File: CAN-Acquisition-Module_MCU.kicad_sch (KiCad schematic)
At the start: 25 parts

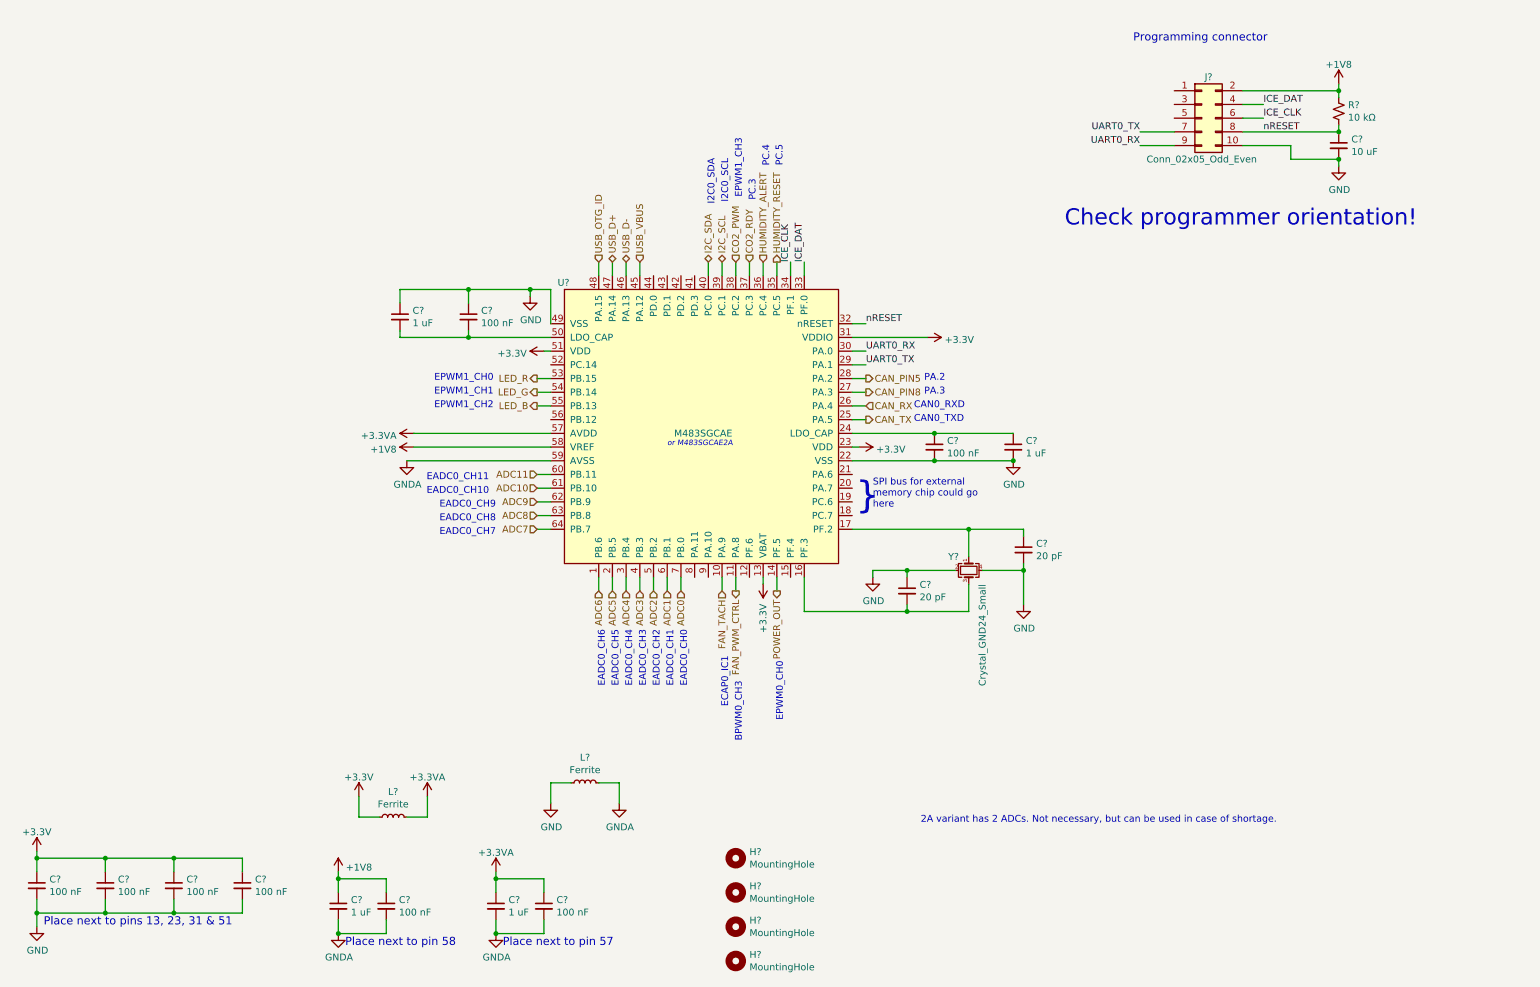
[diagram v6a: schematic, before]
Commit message: Added screen sections and annotations
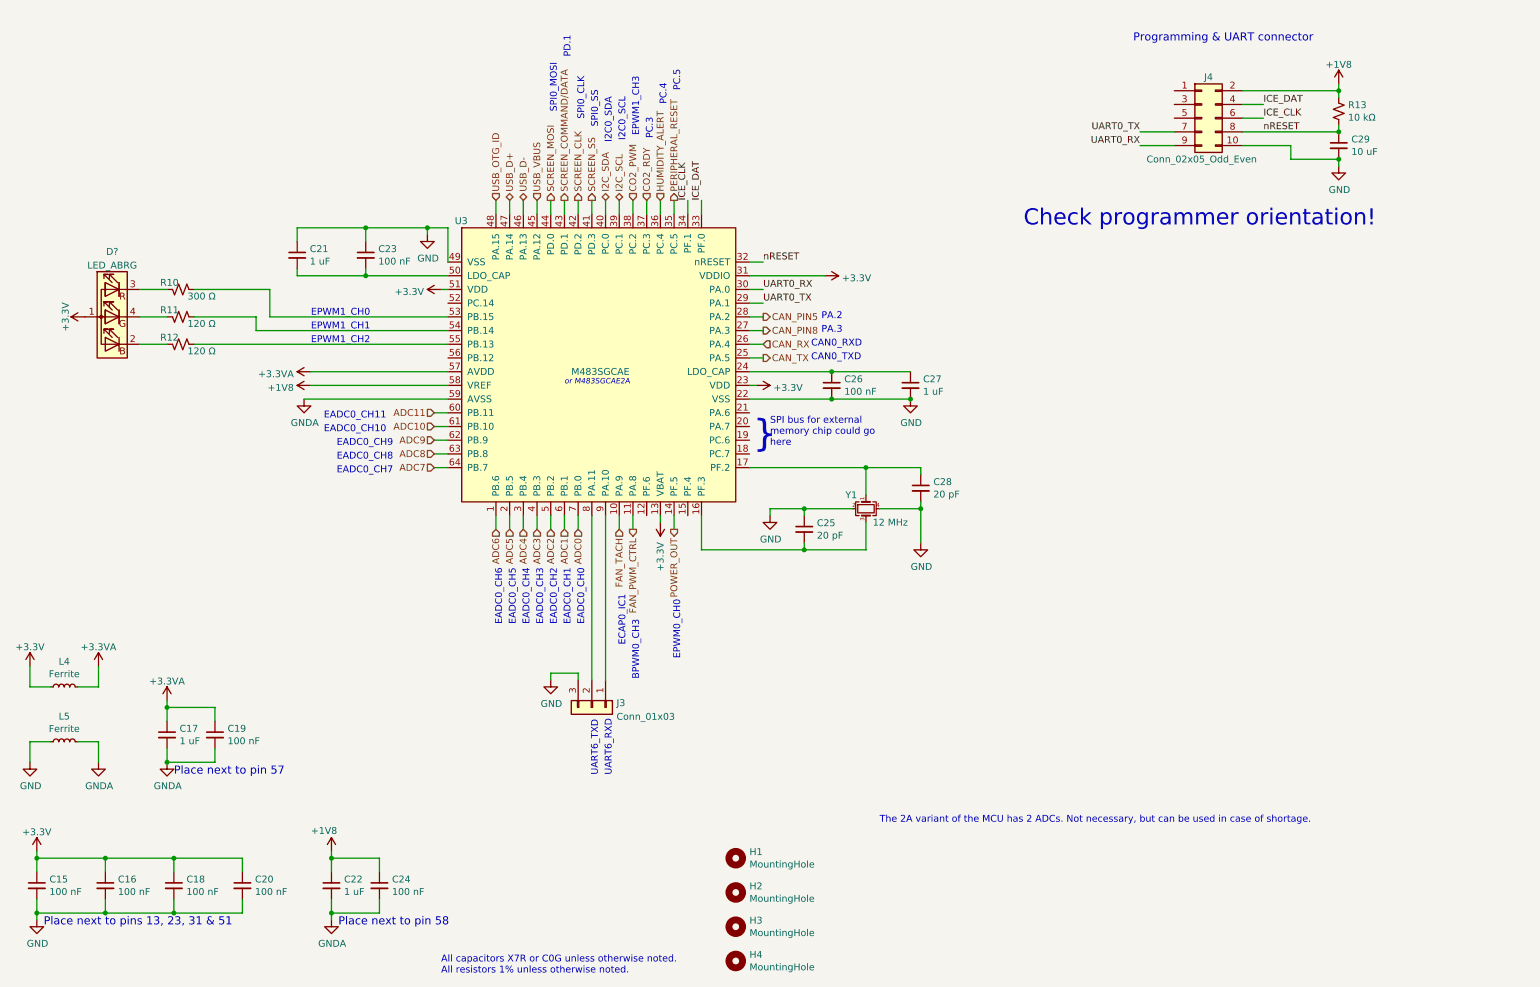
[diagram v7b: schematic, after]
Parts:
- removed H? (x3): MountingHole, symbol Mechanical:MountingHole
- added D?: LED_ABRG, CAN-Acquisition-Module:LED_RGB_Wuerth-PLCC4_3.2x2.8mm_150141M173100, symbol Device:LED_ABRG
- added H2, H3, H4: MountingHole, MountingHole:MountingHole_3.2mm_M3, symbol Mechanical:MountingHole
- added J3: Conn_01x03, Connector_PinHeader_1.27mm:PinHeader_1x03_P1.27mm_Vertical, symbol Connector_Generic:Conn_01x03
- added R10: 300 Ω, Resistor_SMD:R_0603_1608Metric, symbol Device:R_Small_US
- added R11, R12: 120 Ω, Resistor_SMD:R_0603_1608Metric, symbol Device:R_Small_US
- C15, C16, C18, C19, C20, C23, C24, C26: renamed from C?; Mfr. (none) -> KYOCERA AVX; P/N (none) -> 0402YC104KAT2A; Rated Voltage (none) -> 16V
- C17, C21, C22, C27: renamed from C?; Mfr. (none) -> Samsung Electro-Mechanics; P/N (none) -> CL10B105KA8NNNC; Rated Voltage (none) -> 25V
- C29: renamed from C?; footprint Capacitor_SMD:C_1206_3216Metric -> Capacitor_SMD:C_0805_2012Metric; Mfr. (none) -> TDK Corporation; P/N (none) -> C2012X7R0J106K125AB; Rated Voltage (none) -> 6.3V
- H1: renamed from H?; footprint (none) -> MountingHole:MountingHole_3.2mm_M3
- J4: renamed from J?; footprint (none) -> Connector_PinSocket_2.54mm:PinSocket_2x05_P2.54mm_Vertical
- Y1: renamed from Y?; value Crystal_GND24_Small -> 12 MHz
- gave numbers to parts that had none: 6
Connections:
- net +3V3: now also D?.1 (A)
- net GND: now also J3.3 (Pin_3)
- net SCREEN_SS: now reaches U3.41 (PD.3)
- net SCREEN_CLK: now reaches U3.42 (PD.2)
- net SCREEN_COMMAND/DATA: now reaches U3.43 (PD.1)
- net SCREEN_MOSI: now reaches U3.44 (PD.0)
- net at U3.8 (PA.11): now also J3.2 (Pin_2)
- net at U3.9 (PA.10): now also J3.1 (Pin_1)
- net HUMIDITY_RESET renamed PERIPHERAL_RESET
- net LED_B: no longer names the net of U3.55 (PB.13)
- net LED_B: now also R12.1
- net LED_G: no longer names the net of U3.54 (PB.14)
- net LED_G: now also R11.1
- net LED_R: no longer names the net of U3.53 (PB.15)
- net LED_R: now also R10.1
- new net: D?.4 (GK), R11.2
- new net: D?.2 (BK), R12.2
- new net: D?.3 (RK), R10.2
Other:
- note added: "All capacitors X7R or C0G unless otherwise noted. All resistors 1% unless otherwise noted."
- note added: "PD.1"
- note added: "Programming & UART connector"
- note added: "SPI0_CLK"
- note added: "SPI0_MOSI"
- note added: "SPI0_SS"
- note added: "The 2A variant of the MCU has 2 ADCs. Not necessary, but can be used in case of shortage."
- note added: "UART6_RXD"
- note added: "UART6_TXD"
- note removed: "2A variant has 2 ADCs. Not necessary, but can be used in case of shortage."
- note removed: "Programming connector"
- moved on the sheet: C17, C19, C21, C22, C23, C24, C25, C26, C27, C28, L4, L5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

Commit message: PCB started
Placement well advanced
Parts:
- added C43: 1 uF, Capacitor_SMD:C_0603_1608Metric, symbol Device:C_Small
- added C45: 100 nF, Capacitor_SMD:C_0402_1005Metric, symbol Device:C_Small
- gave numbers to parts that had none: 1
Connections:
- net +1V8: no longer J4.2 (Pin_2), R13.1
- net +3V3: now also J4.2 (Pin_2), R13.1, C43.1, C45.1
- net GND: now also C43.2, C45.2
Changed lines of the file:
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@@
   (junction (at 176.53 86.36) (diameter 0) (color 0 0 0 0)
   )
+  (junction (at 27.94 118.11) (diameter 0) (color 0 0 0 0)
+  )
   (junction (at 193.04 106.68) (diameter 0) (color 0 0 0 0)
   )
@@
   (junction (at 53.34 143.51) (diameter 0) (color 0 0 0 0)
   )
+  (junction (at 27.94 107.95) (diameter 0) (color 0 0 0 0)
+  )
   (junction (at 270.51 41.91) (diameter 0) (color 0 0 0 0)
   )
@@
     (stroke (width 0) (type default) (color 0 0 0 0))
   )
+  (wire (pts (xy 36.83 107.95) (xy 27.94 107.95))
+    (stroke (width 0) (type default) (color 0 0 0 0))
+  )
   (wire (pts (xy 161.29 76.2) (xy 163.83 76.2))
     (stroke (width 0) (type default) (color 0 0 0 0))
@@
     (stroke (width 0) (type default) (color 0 0 0 0))
   )
+  (wire (pts (xy 27.94 118.11) (xy 36.83 118.11))
+    (stroke (width 0) (type default) (color 0 0 0 0))
+  )
+  (wire (pts (xy 27.94 110.49) (xy 27.94 107.95))
+    (stroke (width 0) (type default) (color 0 0 0 0))
+  )
   (wire (pts (xy 90.17 63.5) (xy 105.41 63.5))
     (stroke (width 0) (type default) (color 0 0 0 0))
@@
     (stroke (width 0) (type default) (color 0 0 0 0))
   )
+  (wire (pts (xy 27.94 118.11) (xy 27.94 119.38))
+    (stroke (width 0) (type default) (color 0 0 0 0))
+  )
   (wire (pts (xy 121.92 107.95) (xy 121.92 110.49))
     (stroke (width 0) (type default) (color 0 0 0 0))
@@
     (stroke (width 0) (type default) (color 0 0 0 0))
   )
+  (wire (pts (xy 27.94 106.68) (xy 27.94 107.95))
+    (stroke (width 0) (type default) (color 0 0 0 0))
+  )
   (wire (pts (xy 41.91 171.45) (xy 41.91 173.99))
     (stroke (width 0) (type default) (color 0 0 0 0))
@@
     (stroke (width 0) (type default) (color 0 0 0 0))
   )
+  (wire (pts (xy 36.83 110.49) (xy 36.83 107.95))
+    (stroke (width 0) (type default) (color 0 0 0 0))
+  )
   (wire (pts (xy 165.1 106.68) (xy 171.45 106.68))
     (stroke (width 0) (type default) (color 0 0 0 0))
@@
     (stroke (width 0) (type default) (color 0 0 0 0))
   )
+  (wire (pts (xy 27.94 118.11) (xy 27.94 115.57))
+    (stroke (width 0) (type default) (color 0 0 0 0))
+  )
   (wire (pts (xy 92.71 181.61) (xy 92.71 179.07))
     (stroke (width 0) (type default) (color 0 0 0 0))
@@
   )
   (wire (pts (xy 191.135 81.28) (xy 176.53 81.28))
+    (stroke (width 0) (type default) (color 0 0 0 0))
+  )
+  (wire (pts (xy 36.83 118.11) (xy 36.83 115.57))
     (stroke (width 0) (type default) (color 0 0 0 0))
   )
@@
     (pin "1")
   )
+  (symbol (lib_id "power:+3.3V") (at 27.94 106.68 0) (unit 1)
+    (in_bom yes) (on_board yes) (fields_autoplaced)
+    (property "Reference" "#PWR0109" (id 0) (at 27.94 110.49 0)
+      (effects (font (size 1.27 1.27)) hide)
+    )
+    (property "Value" "+3.3V" (id 1) (at 27.94 103.1042 0))
+    (property "Footprint" "" (id 2) (at 27.94 106.68 0)
+      (effects (font (size 1.27 1.27)) hide)
+    )
+    (property "Datasheet" "" (id 3) (at 27.94 106.68 0)
+      (effects (font (size 1.27 1.27)) hide)
+    )
+    (pin "1")
+  )
   (symbol (lib_id "power:+3.3V") (at 162.56 83.82 270) (unit 1)
     (in_bom yes) (on_board yes) (fields_autoplaced)
@@
     (pin "1")
   )
+  (symbol (lib_id "Device:C_Small") (at 36.83 113.03 0) (unit 1)
+    (in_bom yes) (on_board yes)
+    (property "Reference" "C45" (id 0) (at 39.1668 111.8616 0)
+      (effects (font (size 1.27 1.27)) (justify left))
+    )
+    (property "Value" "100 nF" (id 1) (at 39.1668 114.173 0)
+      (effects (font (size 1.27 1.27)) (justify left))
+    )
+    (property "Footprint" "Capacitor_SMD:C_0402_1005Metric" (id 2) (at 36.83 113.03 0)
+      (effects (font (size 1.27 1.27)) hide)
+    )
+    (property "Datasheet" "~" (id 3) (at 36.83 113.03 0)
+      (effects (font (size 1.27 1.27)) hide)
+    )
+    (property "Mfr." "KYOCERA AVX " (id 4) (at 36.83 113.03 0)
+      (effects (font (size 1.27 1.27)) hide)
+    )
+    (property "P/N" "0402YC104KAT2A" (id 5) (at 36.83 113.03 0)
+      (effects (font (size 1.27 1.27)) hide)
+    )
+    (property "Rated Voltage" "16V" (id 6) (at 36.83 113.03 0)
+      (effects (font (size 1.27 1.27)) hide)
+    )
+    (pin "1")
+    (pin "2")
+  )
   (symbol (lib_id "power:GND") (at 124.46 138.43 0) (unit 1)
     (in_bom yes) (on_board yes)
@@
     (pin "1")
   )
-  (symbol (lib_id "power:+1V8") (at 270.51 27.94 0) (unit 1)
-    (in_bom yes) (on_board yes) (fields_autoplaced)
-    (property "Reference" "#PWR059" (id 0) (at 270.51 31.75 0)
-      (effects (font (size 1.27 1.27)) hide)
-    )
-    (property "Value" "+1V8" (id 1) (at 270.51 24.3642 0))
-    (property "Footprint" "" (id 2) (at 270.51 27.94 0)
-      (effects (font (size 1.27 1.27)) hide)
-    )
-    (property "Datasheet" "" (id 3) (at 270.51 27.94 0)
-      (effects (font (size 1.27 1.27)) hide)
-    )
-    (pin "1")
-  )
   (symbol (lib_id "power:+1V8") (at 80.01 83.82 90) (unit 1)
     (in_bom yes) (on_board yes) (fields_autoplaced)
@@
     (pin "1")
   )
+  (symbol (lib_id "Device:C_Small") (at 27.94 113.03 0) (unit 1)
+    (in_bom yes) (on_board yes)
+    (property "Reference" "C43" (id 0) (at 30.2768 111.8616 0)
+      (effects (font (size 1.27 1.27)) (justify left))
+    )
+    (property "Value" "1 uF" (id 1) (at 30.2768 114.173 0)
+      (effects (font (size 1.27 1.27)) (justify left))
+    )
+    (property "Footprint" "Capacitor_SMD:C_0603_1608Metric" (id 2) (at 27.94 113.03 0)
+      (effects (font (size 1.27 1.27)) hide)
+    )
+    (property "Datasheet" "~" (id 3) (at 27.94 113.03 0)
+      (effects (font (size 1.27 1.27)) hide)
+    )
+    (property "Mfr." "Samsung Electro-Mechanics " (id 4) (at 27.94 113.03 0)
+      (effects (font (size 1.27 1.27)) hide)
+    )
+    (property "P/N" "CL10B105KA8NNNC" (id 5) (at 27.94 113.03 0)
+      (effects (font (size 1.27 1.27)) hide)
+    )
+    (property "Rated Voltage" "25V" (id 6) (at 27.94 113.03 0)
+      (effects (font (size 1.27 1.27)) hide)
+    )
+    (pin "1")
+    (pin "2")
+  )
   (symbol (lib_id "Device:C_Small") (at 83.82 176.53 0) (unit 1)
     (in_bom yes) (on_board yes)
@@
     (pin "1")
     (pin "2")
+  )
+  (symbol (lib_id "power:GND") (at 27.94 119.38 0) (unit 1)
+    (in_bom yes) (on_board yes) (fields_autoplaced)
+    (property "Reference" "#PWR0108" (id 0) (at 27.94 125.73 0)
+      (effects (font (size 1.27 1.27)) hide)
+    )
+    (property "Value" "GND" (id 1) (at 27.94 123.8234 0))
+    (property "Footprint" "" (id 2) (at 27.94 119.38 0)
+      (effects (font (size 1.27 1.27)) hide)
+    )
+    (property "Datasheet" "" (id 3) (at 27.94 119.38 0)
+      (effects (font (size 1.27 1.27)) hide)
+    )
+    (pin "1")
   )
   (symbol (lib_id "power:+3.3VA") (at 53.34 142.24 0) (unit 1)
@@
   (symbol (lib_id "Device:LED_ABRG") (at 43.18 71.12 0) (mirror y) (unit 1)
     (in_bom yes) (on_board yes) (fields_autoplaced)
-    (property "Reference" "D?" (id 0) (at 43.18 59.0382 0))
+    (property "Reference" "D7" (id 0) (at 43.18 59.0382 0))
     (property "Value" "LED_ABRG" (id 1) (at 43.18 61.5751 0))
     (property "Footprint" "CAN-Acquisition-Module:LED_RGB_Wuerth-PLCC4_3.2x2.8mm_150141M173100" (id 2) (at 43.18 72.39 0)
@@
       (effects (font (size 1.27 1.27)) hide)
     )
+    (pin "1")
+  )
+  (symbol (lib_id "power:+3.3V") (at 270.51 27.94 0) (unit 1)
+    (in_bom yes) (on_board yes) (fields_autoplaced)
+    (property "Reference" "#PWR0181" (id 0) (at 270.51 31.75 0)
+      (effects (font (size 1.27 1.27)) hide)
+    )
+    (property "Value" "+3.3V" (id 1) (at 271.907 27.1038 0)
+      (effects (font (size 1.27 1.27)) (justify left))
+    )
+    (property "Footprint" "" (id 2) (at 270.51 27.94 0)
+      (effects (font (size 1.27 1.27)) hide)
+    )
+    (property "Datasheet" "" (id 3) (at 270.51 27.94 0)
+      (effects (font (size 1.27 1.27)) hide)
+    )
